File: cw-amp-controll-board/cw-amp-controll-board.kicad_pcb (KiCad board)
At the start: 4 copper layers, 78 x 100 mm, 71 parts, among them J1 Conn_02x07_Odd_Even, J2 Conn_01x06, J3 Conn_02x05_Odd_Even, J4 Conn_01x03_Male, J5 Conn_01x02, Q1 BC850, Q2 BC850, Q3 BC850, Q4 BC850, SW1 RotaryEncoder_Switch, U1 LDL1117S33R, U2 PCF8574, U3 ESP32-C3-WROOM-02, U4 AT42QT2120-CommsMode, U5 PCF8574, U6 PCM5100A

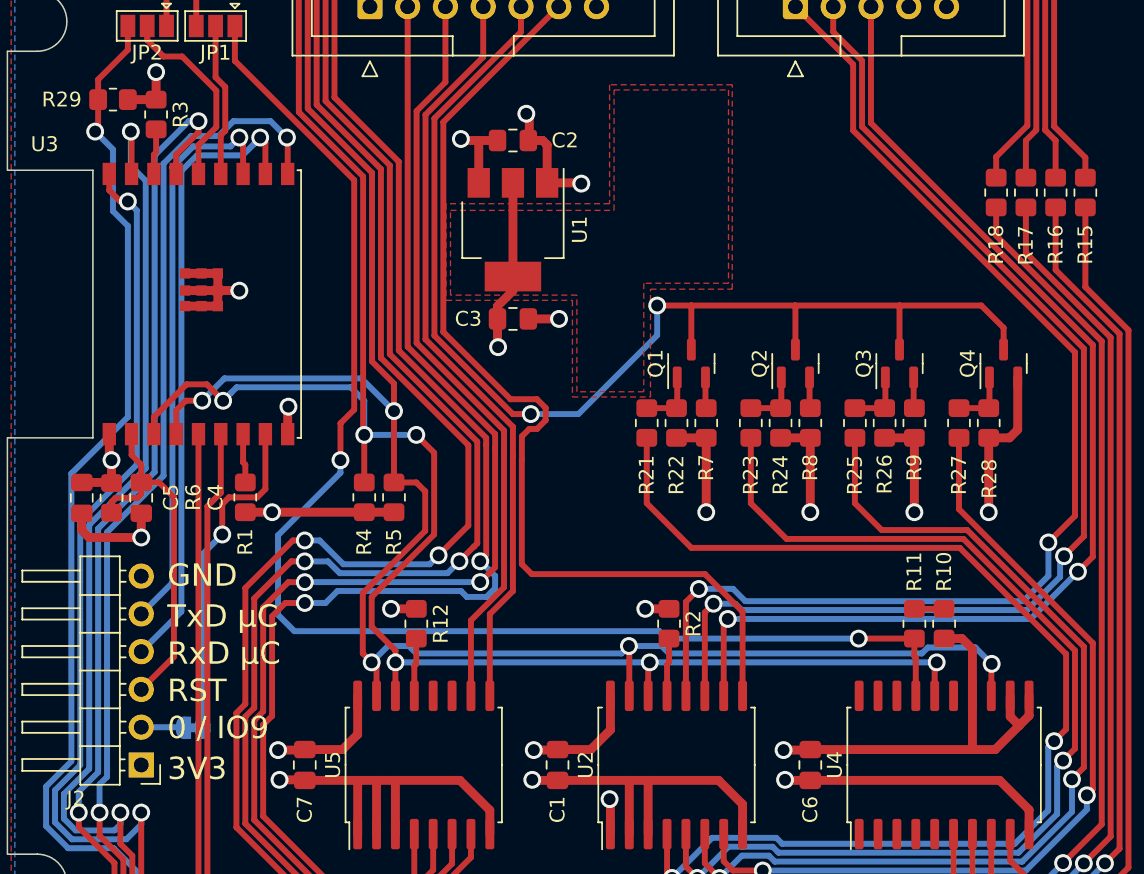
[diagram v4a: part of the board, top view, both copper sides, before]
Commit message: error correction aftertest; corrected pinout touch; added level shifter for i2c poti; corrected voltages i2c poti
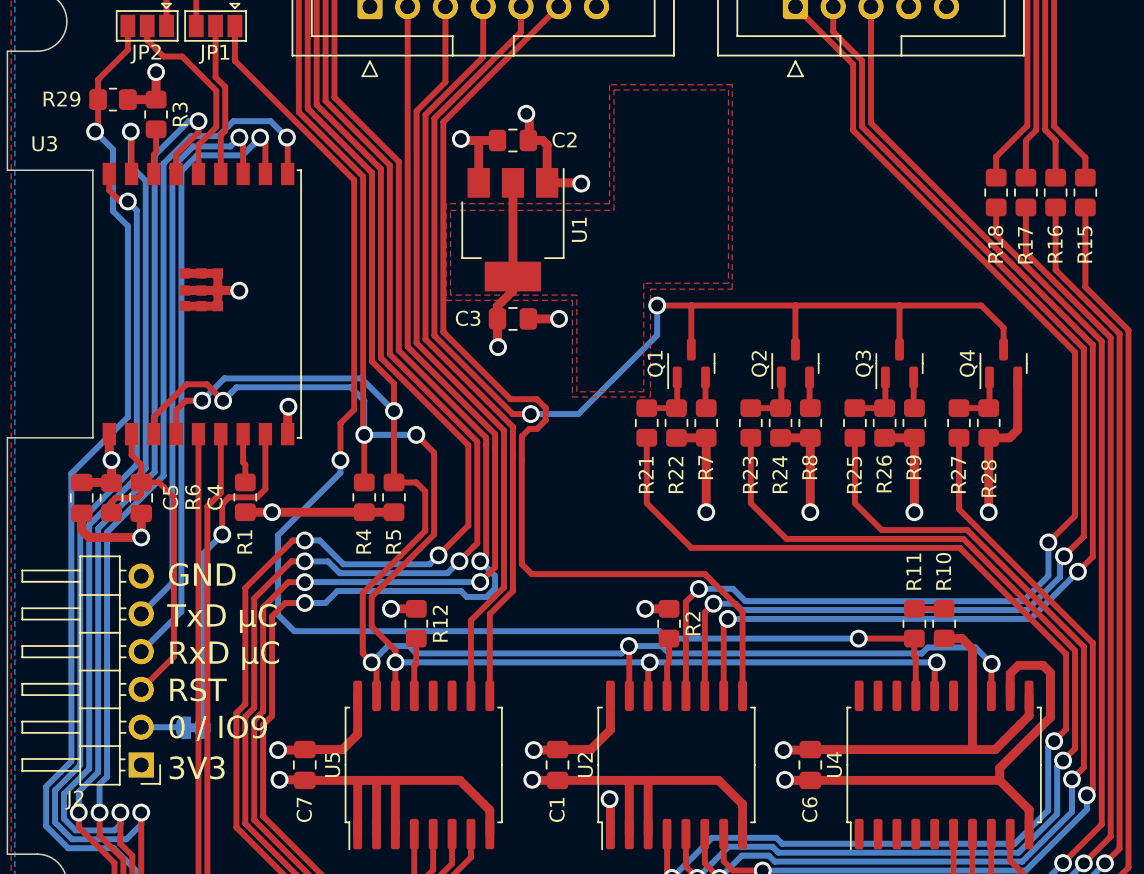
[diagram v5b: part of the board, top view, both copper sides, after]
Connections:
- U4 pad 12: +3V3 -> GNDD
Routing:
- net GNDD: track 526.3 -> 539.6 mm
- net +3V3: track 455.9 -> 453.7 mm
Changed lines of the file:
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@@
       (layerselection 0x00010fc_ffffffff)
       (disableapertmacros false)
-      (usegerberextensions false)
-      (usegerberattributes true)
-      (usegerberadvancedattributes true)
-      (creategerberjobfile true)
+      (usegerberextensions true)
+      (usegerberattributes false)
+      (usegerberadvancedattributes false)
+      (creategerberjobfile false)
       (svguseinch false)
       (svgprecision 6)
@@
       (psa4output false)
       (plotreference true)
-      (plotvalue true)
+      (plotvalue false)
       (plotinvisibletext false)
       (sketchpadsonfab false)
-      (subtractmaskfromsilk false)
+      (subtractmaskfromsilk true)
       (outputformat 1)
       (mirror false)
-      (drillshape 1)
+      (drillshape 0)
       (scaleselection 1)
-      (outputdirectory "")
+      (outputdirectory "export")
     )
   )
@@
   (net 74 "/BT-PREV-P2")
   (net 75 "/BT-ON-OFF-P3")
-  (net 76 "Net-(U3-Pad13)")
-  (net 77 "Net-(U3-Pad14)")
+  (net 76 "Net-(JP1-Pad2)")
+  (net 77 "Net-(JP2-Pad2)")
   (net 78 "ROTARY-SWITCH")
   (footprint "Connector_IDC:IDC-Header_2x05_P2.54mm_Vertical" (layer "F.Cu")
@@
       (net 40 "~{TOUCH-INT}") (pinfunction "A") (pintype "passive"))
     (pad "2" smd rect (at 0 0 180) (size 1 1.5) (layers "F.Cu" "F.Mask")
-      (net 76 "Net-(U3-Pad13)") (pinfunction "C") (pintype "passive"))
+      (net 76 "Net-(JP1-Pad2)") (pinfunction "C") (pintype "passive"))
     (pad "3" smd rect (at 1.3 0 180) (size 1 1.5) (layers "F.Cu" "F.Mask")
       (net 52 "Net-(J5-Pad1)") (pinfunction "B") (pintype "passive"))
@@
       (net 1 "+3V3") (pinfunction "VDD") (pintype "power_in"))
     (pad "12" smd roundrect (at 4.65 4.445 90) (size 2.05 0.6) (layers "F.Cu" "F.Paste" "F.Mask") (roundrect_rratio 0.25)
-      (net 1 "+3V3") (pinfunction "MODE") (pintype "input"))
+      (net 2 "GNDD") (pinfunction "MODE") (pintype "input"))
     (pad "13" smd roundrect (at 4.65 3.175 90) (size 2.05 0.6) (layers "F.Cu" "F.Paste" "F.Mask") (roundrect_rratio 0.25)
       (net 19 "SDA") (pinfunction "SDA") (pintype "bidirectional"))
@@
       (net 53 "Net-(J5-Pad2)") (pinfunction "A") (pintype "passive"))
     (pad "2" smd rect (at 0 0 180) (size 1 1.5) (layers "F.Cu" "F.Mask")
-      (net 77 "Net-(U3-Pad14)") (pinfunction "C") (pintype "passive"))
+      (net 77 "Net-(JP2-Pad2)") (pinfunction "C") (pintype "passive"))
     (pad "3" smd rect (at 1.3 0 180) (size 1 1.5) (layers "F.Cu" "F.Mask")
       (net 78 "ROTARY-SWITCH") (pinfunction "B") (pintype "passive"))
@@
     (fp_line (start -1 0.625) (end -1 -0.625) (layer "F.Fab") (width 0.1))
     (fp_line (start 1 0.625) (end -1 0.625) (layer "F.Fab") (width 0.1))
-    (pad "1" smd roundrect (at -1 0) (size 1.2 1.4) (layers "F.Cu" "F.Paste" "F.Mask") (roundrect_rratio 0.208333)
+    (pad "1" smd roundrect (at -1 0) (size 1.2 1.4) (layers "F.Cu" "F.Paste" "F.Mask") (roundrect_rratio 0.2083333333)
       (net 78 "ROTARY-SWITCH") (pintype "passive"))
-    (pad "2" smd roundrect (at 1 0) (size 1.2 1.4) (layers "F.Cu" "F.Paste" "F.Mask") (roundrect_rratio 0.208333)
+    (pad "2" smd roundrect (at 1 0) (size 1.2 1.4) (layers "F.Cu" "F.Paste" "F.Mask") (roundrect_rratio 0.2083333333)
       (net 1 "+3V3") (pintype "passive"))
     (model "${KICAD6_3DMODEL_DIR}/Resistor_SMD.3dshapes/R_0805_2012Metric.wrl"
@@
       (net 24 "µC-TXD") (pinfunction "GPIO21/U0TXD") (pintype "bidirectional"))
     (pad "13" smd rect (at 8.75 3.35 270) (size 1.5 0.9) (layers "F.Cu" "F.Paste" "F.Mask")
-      (net 76 "Net-(U3-Pad13)") (pinfunction "GPIO18/USB_D-") (pintype "bidirectional"))
+      (net 76 "Net-(JP1-Pad2)") (pinfunction "GPIO18/USB_D-") (pintype "bidirectional"))
     (pad "14" smd rect (at 8.75 1.85 270) (size 1.5 0.9) (layers "F.Cu" "F.Paste" "F.Mask")
-      (net 77 "Net-(U3-Pad14)") (pinfunction "GPIO19/USB_D+") (pintype "bidirectional"))
+      (net 77 "Net-(JP2-Pad2)") (pinfunction "GPIO19/USB_D+") (pintype "bidirectional"))
     (pad "15" smd rect (at 8.75 0.35 270) (size 1.5 0.9) (layers "F.Cu" "F.Paste" "F.Mask")
       (net 54 "LRCLK") (pinfunction "GPIO3/ADC1_CH3") (pintype "bidirectional"))
@@
   (segment (start 180.715 115.685) (end 180.05 116.35) (width 0.6) (layer "F.Cu") (net 1))
   (segment (start 116.4 151.075) (end 119.5 151.075) (width 0.4) (layer "F.Cu") (net 1))
-  (segment (start 179.445 115.745) (end 180.05 116.35) (width 0.6) (layer "F.Cu") (net 1))
   (segment (start 131.5 143.975) (end 130.6 143.975) (width 0.4) (layer "F.Cu") (net 1))
   (segment (start 128.3625 149.4) (end 127.175 149.4) (width 0.4) (layer "F.Cu") (net 1))
@@
   (segment (start 122.6375 149.4) (end 121.275 149.4) (width 0.4) (layer "F.Cu") (net 1))
   (segment (start 136 102) (end 138 102) (width 0.6) (layer "F.Cu") (net 1))
-  (segment (start 179.445 114.35) (end 179.445 115.745) (width 0.6) (layer "F.Cu") (net 1))
   (segment (start 126.5 140.475) (end 126.5 138.775) (width 0.6) (layer "F.Cu") (net 1))
   (segment (start 130.6 143.975) (end 129.725 144.85) (width 0.4) (layer "F.Cu") (net 1))
@@
   (segment (start 155.095 123.65) (end 155.095 120.060617) (width 0.6) (layer "F.Cu") (net 2))
   (segment (start 149 120.0375) (end 147.3375 120.0375) (width 0.6) (layer "F.Cu") (net 2))
+  (segment (start 178.7375 120.0375) (end 178.7375 119.2125) (width 0.6) (layer "F.Cu") (net 2))
   (segment (start 166 120.0375) (end 178.7375 120.0375) (width 0.6) (layer "F.Cu") (net 2))
   (segment (start 147.1 75.4) (end 147.1 76.9375) (width 0.6) (layer "F.Cu") (net 2))
   (segment (start 135.555 123.65) (end 135.555 120.045) (width 0.6) (layer "F.Cu") (net 2))
   (segment (start 117 103.2) (end 117 102.075) (width 0.6) (layer "F.Cu") (net 2))
+  (segment (start 182.15 115.8) (end 182.15 112.8) (width 0.6) (layer "F.Cu") (net 2))
   (segment (start 124.4 141.7875) (end 124.4 143.475) (width 0.6) (layer "F.Cu") (net 2))
+  (segment (start 178.7375 119.2125) (end 182.15 115.8) (width 0.6) (layer "F.Cu") (net 2))
   (segment (start 179.95 96.45) (end 179.4 97) (width 0.6) (layer "F.Cu") (net 2))
   (segment (start 180.715 122.015) (end 180.715 123.65) (width 0.6) (layer "F.Cu") (net 2))
@@
   (segment (start 179.95 92.9375) (end 179.95 96.45) (width 0.6) (layer "F.Cu") (net 2))
   (segment (start 117.5 147.4375) (end 117.5 145.9745) (width 0.6) (layer "F.Cu") (net 2))
+  (segment (start 179.445 112.855) (end 179.445 114.35) (width 0.6) (layer "F.Cu") (net 2))
   (segment (start 124.425 141.7625) (end 124.4 141.7875) (width 0.6) (layer "F.Cu") (net 2))
   (segment (start 155.118117 120.0375) (end 159.8375 120.0375) (width 0.6) (layer "F.Cu") (net 2))
@@
   (segment (start 135.555 120.045) (end 135.5625 120.0375) (width 0.6) (layer "F.Cu") (net 2))
   (segment (start 136.830581 120.0375) (end 138.080229 120.0375) (width 0.6) (layer "F.Cu") (net 2))
+  (segment (start 181.65 112.3) (end 180 112.3) (width 0.6) (layer "F.Cu") (net 2))
   (segment (start 122.6375 148.75) (end 124.025 148.75) (width 0.4) (layer "F.Cu") (net 2))
   (segment (start 130.85 94.95) (end 130.9 94.9) (width 0.6) (layer "F.Cu") (net 2))
@@
   (segment (start 128.3625 148.1) (end 124.4 148.1) (width 0.4) (layer "F.Cu") (net 2))
   (segment (start 123.95 88.14) (end 125.05 88.14) (width 0.6) (layer "F.Cu") (net 2))
+  (segment (start 182.15 112.8) (end 181.65 112.3) (width 0.6) (layer "F.Cu") (net 2))
   (segment (start 148 77) (end 147.0375 77) (width 0.6) (layer "F.Cu") (net 2))
   (segment (start 144.445 122.045) (end 144.445 123.65) (width 0.6) (layer "F.Cu") (net 2))
@@
   (segment (start 117.5 103.7) (end 117 103.2) (width 0.6) (layer "F.Cu") (net 2))
   (segment (start 124.475 143.55) (end 124.4 143.475) (width 0.4) (layer "F.Cu") (net 2))
+  (segment (start 180 112.3) (end 179.445 112.855) (width 0.6) (layer "F.Cu") (net 2))
   (segment (start 123.95 85.94) (end 125.05 85.94) (width 0.6) (layer "F.Cu") (net 2))
   (segment (start 150.55 79.85) (end 150.6 79.9) (width 0.6) (layer "F.Cu") (net 2))

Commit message: layout v1.2
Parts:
- removed Q1, Q2, Q3, Q4: BC850, Package_TO_SOT_SMD:SOT-23
- removed R22, R24, R26, R28: 10k, Resistor_SMD:R_0805_2012Metric_Pad1.20x1.40mm_HandSolder
- removed R7: 51k, Resistor_SMD:R_0805_2012Metric_Pad1.20x1.40mm_HandSolder
- removed R8: 33k, Resistor_SMD:R_0805_2012Metric_Pad1.20x1.40mm_HandSolder
- removed R9: 9k1, Resistor_SMD:R_0805_2012Metric_Pad1.20x1.40mm_HandSolder
- added C19: 100nF, Capacitor_SMD:C_0805_2012Metric_Pad1.18x1.45mm_HandSolder, F.Cu at (162.6, 91.5)
- added U7: 7400, Package_SO:SOIC-14_3.9x8.7mm_P1.27mm, F.Cu at (162.7, 97.6)
- R21: value 10k -> 51K
- R23: value 10k -> 33K
- R25: value 10k -> 9K1
- R27: value 10k -> 0R
- moved R21 19.6 mm to (174.6, 96.4)
- moved R23 14.6 mm to (176.6, 96.4)
- moved R25 9.61 mm to (178.6, 96.4)
- moved R27 4.62 mm to (180.6, 96.4)
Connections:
- R21 pad 2: /BT-PAUSE-Q1 -> BT-KEY
- R23 pad 2: /BT-NEXT-Q2 -> BT-KEY
- R25 pad 2: /BT-PREV-Q3 -> BT-KEY
- R27 pad 2: /BT-ON-OFF-Q4 -> BT-KEY
- U5 pad 10: SELECT-BT -> /~{SELECT-BT}
- U5 pad 5: ~{AMP-Mute} -> /AMP-MUTE
- U5 pad 9: SELECT-Analog -> /~{SELECT-Analog}
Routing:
- net /AMP-MUTE: track 0.00 -> 80.9 mm, vias 0 -> 2
- net +5V: track 18.7 -> 67.5 mm, vias 1 -> 2
- net /~{SELECT-Analog}: track 0.00 -> 48.0 mm, vias 0 -> 2
- net /~{SELECT-BT}: track 0.00 -> 41.4 mm, vias 0 -> 2
- net ~{AMP-Mute}: track 88.5 -> 58.9 mm
- net GNDD: track 539.6 -> 515.0 mm, vias 16 -> 13
- net /BT-PAUSE-P0: track 78.4 -> 59.3 mm
- net /BT-NEXT-P1: track 71.4 -> 58.0 mm
- net /BT-PREV-P2: track 64.5 -> 56.7 mm
- net SELECT-Analog: track 51.0 -> 58.1 mm, vias 0 -> 2
- net /BT-PREV-Q3: track 4.08 -> 0.00 mm
- net /BT-PAUSE-Q1: track 4.08 -> 0.00 mm
- net /BT-ON-OFF-Q4: track 4.08 -> 0.00 mm
- net /BT-NEXT-Q2: track 4.08 -> 0.00 mm
- net BT-MUTE: track 67.4 -> 64.5 mm
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
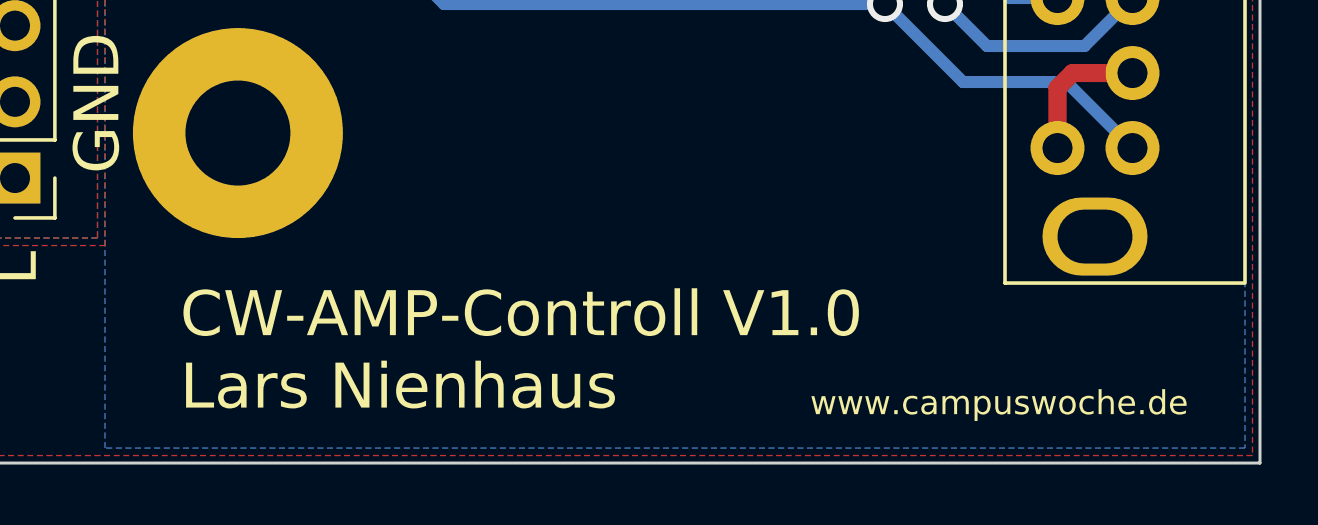
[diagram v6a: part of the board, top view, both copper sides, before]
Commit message: updated Version label
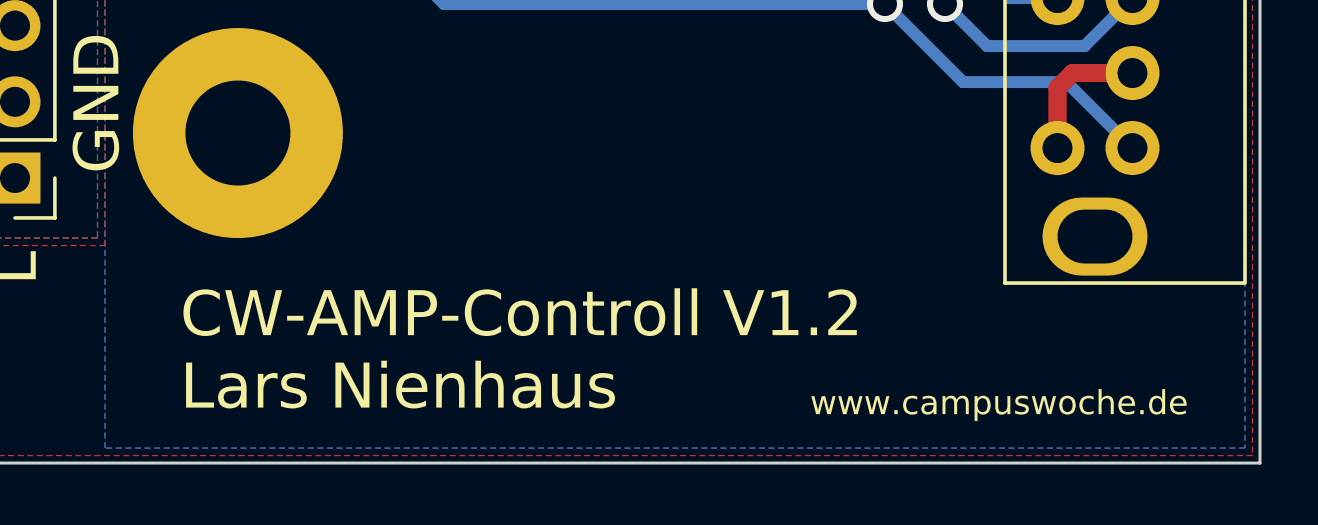
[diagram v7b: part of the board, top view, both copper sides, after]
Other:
- board text added: "CW-AMP-Controll V1.2 Lars Nienhaus"
- board text removed: "CW-AMP-Controll V1.0 Lars Nienhaus"
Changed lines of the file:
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@@
       ))
   )
-  (gr_line (start 114.2 153.2) (end 113.8 153.2)
+  (gr_line (start 168.1 151.8) (end 167.7 151.8)
     (stroke (width 0.15) (type solid)) (layer "B.SilkS"))
-  (gr_line (start 116.7 151) (end 115.3 151)
+  (gr_line (start 170.6 149.6) (end 169.2 149.6)
     (stroke (width 0.15) (type solid)) (layer "B.SilkS"))
-  (gr_line (start 115.3 148.8) (end 115.3 153.2)
+  (gr_line (start 169.2 147.4) (end 169.2 151.8)
     (stroke (width 0.15) (type solid)) (layer "B.SilkS"))
-  (gr_line (start 113.8 153.2) (end 115.3 151.4)
+  (gr_line (start 167.7 151.8) (end 169.2 150)
     (stroke (width 0.15) (type solid)) (layer "B.SilkS"))
-  (gr_line (start 117.4 147.8) (end 117.4 148.8)
+  (gr_line (start 171.3 146.4) (end 171.3 147.4)
     (stroke (width 0.15) (type solid)) (layer "B.SilkS"))
-  (gr_line (start 113.8 148.8) (end 115.3 150.6)
+  (gr_line (start 167.7 147.4) (end 169.2 149.2)
     (stroke (width 0.15) (type solid)) (layer "B.SilkS"))
-  (gr_line (start 116.7 153.2) (end 118.1 153.2)
+  (gr_line (start 170.6 151.8) (end 172 151.8)
     (stroke (width 0.15) (type solid)) (layer "B.SilkS"))
-  (gr_line (start 118.1 153.2) (end 118.1 148.8)
+  (gr_line (start 172 151.8) (end 172 147.4)
     (stroke (width 0.15) (type solid)) (layer "B.SilkS"))
-  (gr_line (start 118.1 148.8) (end 116.7 148.8)
+  (gr_line (start 172 147.4) (end 170.6 147.4)
     (stroke (width 0.15) (type solid)) (layer "B.SilkS"))
-  (gr_line (start 117.4 154.2) (end 117.4 153.2)
+  (gr_line (start 171.3 152.8) (end 171.3 151.8)
     (stroke (width 0.15) (type solid)) (layer "B.SilkS"))
-  (gr_line (start 116.7 148.8) (end 116.7 153.2)
+  (gr_line (start 170.6 147.4) (end 170.6 151.8)
     (stroke (width 0.15) (type solid)) (layer "B.SilkS"))
-  (gr_line (start 113.8 152.7) (end 113.8 153.2)
+  (gr_line (start 167.7 151.3) (end 167.7 151.8)
     (stroke (width 0.15) (type solid)) (layer "B.SilkS"))
   (gr_line (start 112 129) (end 112 158)
@@
     (effects (font (size 1.5 1.5) (thickness 0.3)) (justify left mirror))
   )
-  (gr_text "42Volt.de" (at 116 155.6) (layer "B.SilkS")
+  (gr_text "42Volt.de" (at 169.9 154.2) (layer "B.SilkS")
     (effects (font (size 0.8 0.8) (thickness 0.15)) (justify mirror))
   )
@@
     (effects (font (size 0.8 0.8) (thickness 0.15)) (justify left))
   )
-  (gr_text "CW-AMP-Controll V1.0\nLars Nienhaus" (at 154 154.25) (layer "F.SilkS")
+  (gr_text "CW-AMP-Controll V1.2\nLars Nienhaus" (at 154 154.25) (layer "F.SilkS")
     (effects (font (size 1.5 1.5) (thickness 0.3)) (justify left))
   )
